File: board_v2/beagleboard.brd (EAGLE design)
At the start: 69.8 x 54.6 mm, 40 parts, among them U1 DWM1000, X1 5566-2, X2 04-JST-B4B-XH-A

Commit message: pullups
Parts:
- added R16, R17: 10k, rcl:R0805
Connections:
- net +5V: now also R16.2, R17.2
- net MLEN: now also R17.1
- net MREN: now also R16.1
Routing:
- net +5V: track 174.5 -> 185.0 mm
- net MLEN: track 40.1 -> 43.1 mm
- net MREN: track 44.2 -> 47.0 mm
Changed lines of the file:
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@@
 <element name="R14" library="rcl" package="R0805" value="" x="33.02" y="46.99" rot="R270"/>
 <element name="R15" library="rcl" package="R0805" value="" x="31.115" y="46.99" rot="R90"/>
+<element name="R16" library="rcl" package="R0805" value="10k" x="26.3525" y="20.0025" rot="R180"/>
+<element name="R17" library="rcl" package="R0805" value="10k" x="16.51" y="37.1475" rot="R270"/>
 </elements>
 <signals>
@@
 <wire x1="17.145" y1="10.4775" x2="12.7" y2="6.0325" width="0.8128" layer="16"/>
 <wire x1="12.7" y1="6.0325" x2="12.7" y2="5.08" width="0.8128" layer="16"/>
+<contactref element="R16" pad="2"/>
+<contactref element="R17" pad="2"/>
+<wire x1="16.51" y1="36.1975" x2="17.465" y2="36.1975" width="0.4064" layer="1"/>
+<wire x1="17.465" y1="36.1975" x2="17.78" y2="36.5125" width="0.4064" layer="1"/>
+<wire x1="17.78" y1="36.5125" x2="22.86" y2="36.5125" width="0.4064" layer="1"/>
+<wire x1="22.86" y1="36.5125" x2="23.8125" y2="37.465" width="0.4064" layer="1"/>
+<wire x1="25.4025" y1="20.0025" x2="25.4025" y2="22.3545" width="0.4064" layer="1"/>
+<wire x1="25.4025" y1="22.3545" x2="25.5905" y2="22.5425" width="0.4064" layer="1"/>
 </signal>
 <signal name="CSN">
@@
 <wire x1="40.3225" y1="39.0525" x2="20.6375" y2="39.0525" width="0.4064" layer="1"/>
 <wire x1="20.6375" y1="39.0525" x2="19.3675" y2="37.7825" width="0.4064" layer="1"/>
+<contactref element="R17" pad="1"/>
+<wire x1="16.51" y1="38.0975" x2="19.0525" y2="38.0975" width="0.4064" layer="1"/>
+<wire x1="19.0525" y1="38.0975" x2="19.3675" y2="37.7825" width="0.4064" layer="1"/>
 </signal>
 <signal name="MOSI">
@@
 <wire x1="32.385" y1="20.955" x2="31.4325" y2="20.0025" width="0.4064" layer="1"/>
 <wire x1="31.4325" y1="20.0025" x2="30.1625" y2="20.0025" width="0.4064" layer="1"/>
+<contactref element="R16" pad="1"/>
+<wire x1="27.3025" y1="20.0025" x2="30.1625" y2="20.0025" width="0.4064" layer="1"/>
 </signal>
 <signal name="DWMRES">

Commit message: values
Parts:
- R10, R12, R14: value (none) -> 1,1k
- R11, R13, R15: value (none) -> 2k
- R4, R5, R6: value (none) -> 1k
- R7, R8, R9: value (none) -> 1,5k
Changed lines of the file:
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@@
 <element name="SENS2" library="libsjst_eph" package="B4B-PH-K-S" value="4PIN" x="20.32" y="43.18" rot="R180"/>
 <element name="X2" library="bt_con-jst-xh" package="B4B-XH" value="04-JST-B4B-XH-A" x="69.85" y="34.925" rot="R90"/>
-<element name="R4" library="rcl" package="R0805" value="" x="60.0075" y="33.655"/>
-<element name="R5" library="rcl" package="R0805" value="" x="60.0075" y="31.75"/>
-<element name="R6" library="rcl" package="R0805" value="" x="58.1025" y="27.94"/>
-<element name="R7" library="rcl" package="R0805" value="" x="64.77" y="29.845"/>
-<element name="R8" library="rcl" package="R0805" value="" x="64.77" y="31.75"/>
-<element name="R9" library="rcl" package="R0805" value="" x="64.77" y="33.655"/>
+<element name="R4" library="rcl" package="R0805" value="1k" x="60.0075" y="33.655"/>
+<element name="R5" library="rcl" package="R0805" value="1k" x="60.0075" y="31.75"/>
+<element name="R6" library="rcl" package="R0805" value="1k" x="58.1025" y="27.94"/>
+<element name="R7" library="rcl" package="R0805" value="1,5k" x="64.77" y="29.845"/>
+<element name="R8" library="rcl" package="R0805" value="1,5k" x="64.77" y="31.75"/>
+<element name="R9" library="rcl" package="R0805" value="1,5k" x="64.77" y="33.655"/>
 <element name="SENS1" library="libsjst_eph" package="B4B-PH-K-S" value="4PIN" x="8.5725" y="43.18" rot="R180"/>
 <element name="SENS3" library="libsjst_eph" package="B4B-PH-K-S" value="4PIN" x="32.0675" y="43.18" rot="R180"/>
@@
 <element name="SJ5" library="jumper" package="SJ" value="" x="26.3525" y="25.0825" rot="R180"/>
 <element name="SJ6" library="jumper" package="SJ" value="" x="26.3525" y="27.6225" rot="R180"/>
-<element name="R10" library="rcl" package="R0805" value="" x="9.525" y="46.99" rot="R270"/>
-<element name="R11" library="rcl" package="R0805" value="" x="7.62" y="46.99" rot="R90"/>
-<element name="R12" library="rcl" package="R0805" value="" x="21.2725" y="46.99" rot="R270"/>
-<element name="R13" library="rcl" package="R0805" value="" x="19.3675" y="46.99" rot="R90"/>
-<element name="R14" library="rcl" package="R0805" value="" x="33.02" y="46.99" rot="R270"/>
-<element name="R15" library="rcl" package="R0805" value="" x="31.115" y="46.99" rot="R90"/>
+<element name="R10" library="rcl" package="R0805" value="1,1k" x="9.525" y="46.99" rot="R270"/>
+<element name="R11" library="rcl" package="R0805" value="2k" x="7.62" y="46.99" rot="R90"/>
+<element name="R12" library="rcl" package="R0805" value="1,1k" x="21.2725" y="46.99" rot="R270"/>
+<element name="R13" library="rcl" package="R0805" value="2k" x="19.3675" y="46.99" rot="R90"/>
+<element name="R14" library="rcl" package="R0805" value="1,1k" x="33.02" y="46.99" rot="R270"/>
+<element name="R15" library="rcl" package="R0805" value="2k" x="31.115" y="46.99" rot="R90"/>
 <element name="R16" library="rcl" package="R0805" value="10k" x="26.3525" y="20.0025" rot="R180"/>
 <element name="R17" library="rcl" package="R0805" value="10k" x="16.51" y="37.1475" rot="R270"/>

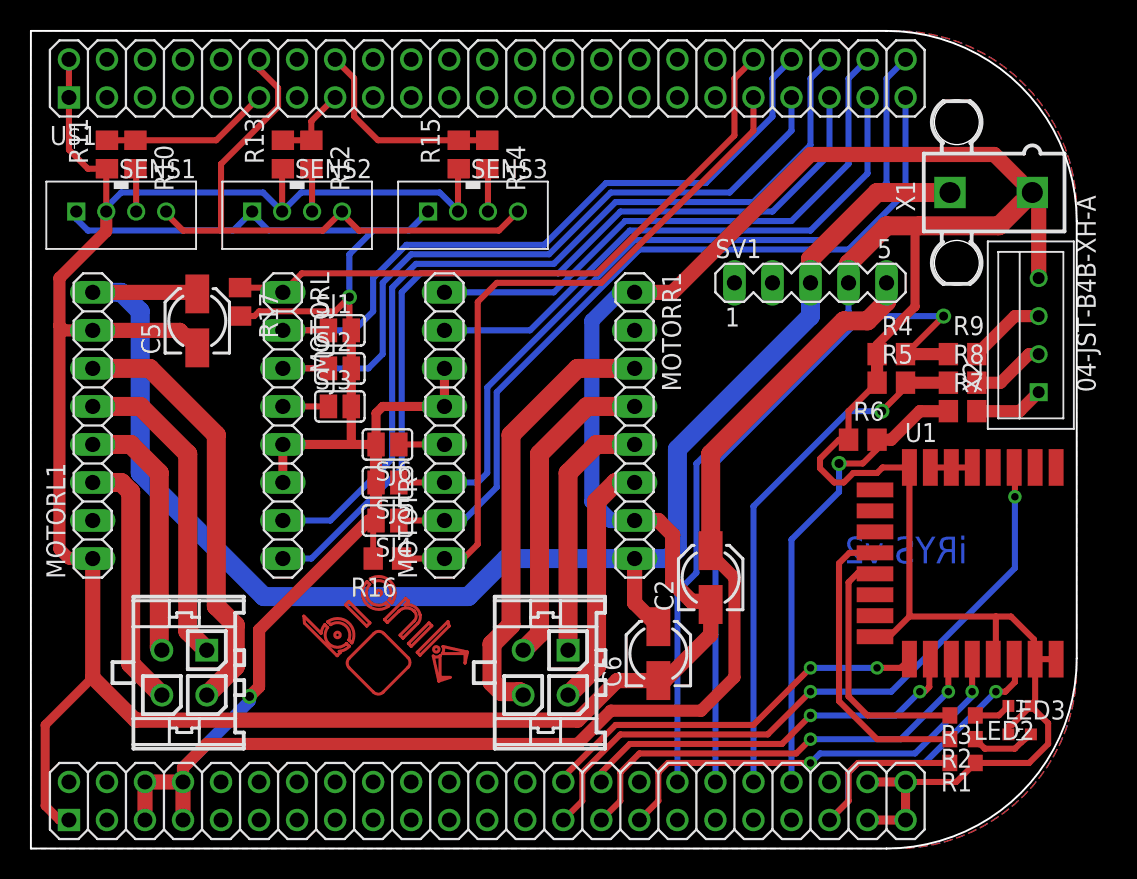
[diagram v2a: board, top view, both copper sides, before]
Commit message: right sonar wires
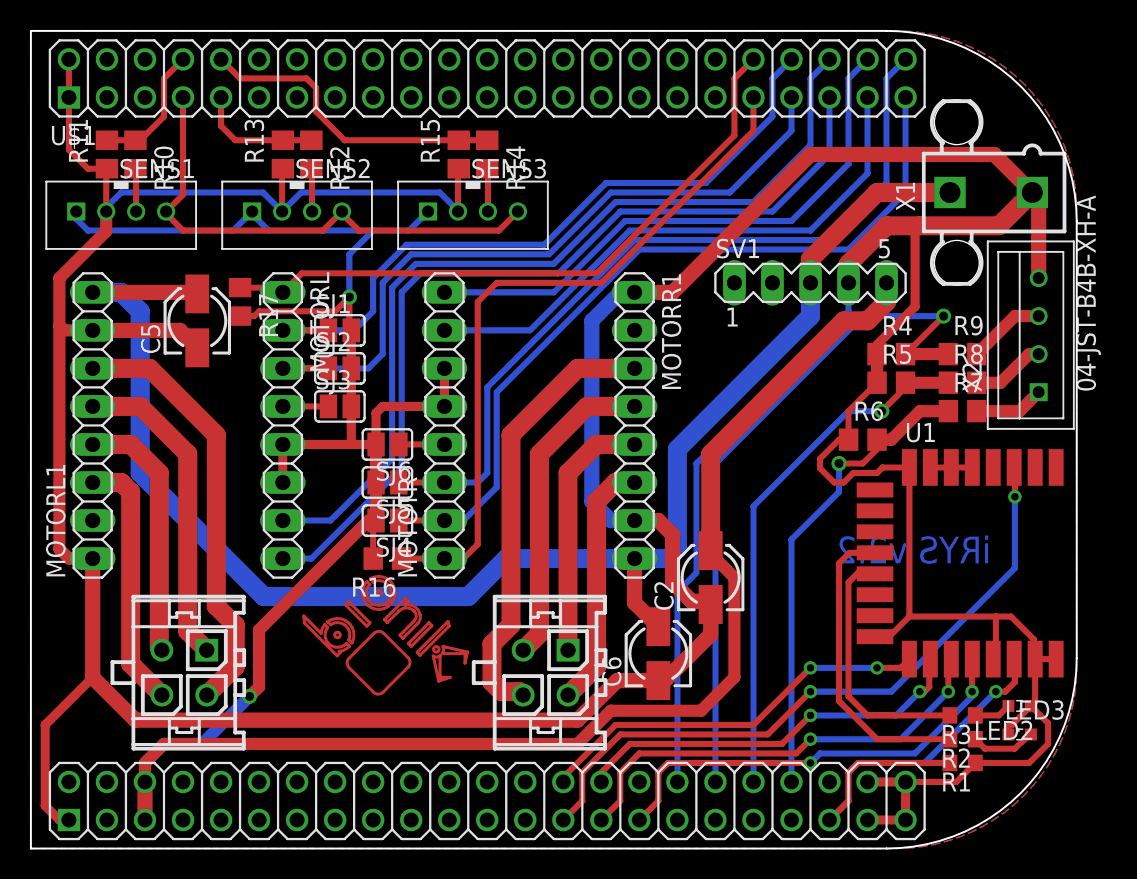
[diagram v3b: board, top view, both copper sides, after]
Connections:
- removed net N$42: U$1.9
- new net N$26: U$1.15
- new net SYS_5V: U$1.53
- net +5V: no longer U$1.53, U$1.54
- net D1ECHO: now also U$1.8; no longer U$1.11
- net D2ECHO: now also U$1.9; no longer U$1.15
- net D3ECHO: now also U$1.10; no longer U$1.16
- net N$20: now also U$1.12; no longer U$1.7
- net N$22: now also U$1.16; no longer U$1.8
- net N$23: now also U$1.11; no longer U$1.10
- net TRIG: now also U$1.7; no longer U$1.12
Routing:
- net D3ECHO: track 13.9 -> 20.9 mm
- net TRIG: track 39.3 -> 33.9 mm
- net D2ECHO: track 5.42 -> 8.33 mm
- net D1ECHO: track 11.3 -> 8.80 mm
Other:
- board text added: "iRYS v2.2"
- board text removed: "iRYS v2"
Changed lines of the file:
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@@
 <board>
 <plain>
-<text x="65.0875" y="19.685" size="1.778" layer="16" rot="MR0">iRYS v2</text>
+<text x="66.675" y="19.685" size="1.778" layer="16" rot="MR0">iRYS v2.2</text>
 <circle x="29.617984375" y="13.93655" radius="0.182878125" width="0.203" layer="1"/>
 <circle x="25.77360625" y="17.704809375" radius="0.18288125" width="0.203" layer="1"/>
@@
 <contactref element="MOTOTR" pad="5"/>
 <contactref element="U$1" pad="52"/>
-<contactref element="U$1" pad="54"/>
 <contactref element="U$1" pad="51"/>
-<contactref element="U$1" pad="53"/>
 <wire x1="30.1625" y1="30.1625" x2="30.1625" y2="32.7025" width="0.6096" layer="1"/>
 <contactref element="C2" pad="+"/>
@@
 <wire x1="47.9425" y1="26.9875" x2="47.9425" y2="20.5325" width="1.27" layer="1"/>
 <wire x1="10.16" y1="2.54" x2="10.16" y2="5.08" width="1.016" layer="1"/>
-<wire x1="10.16" y1="5.08" x2="12.7" y2="5.08" width="1.016" layer="1"/>
-<wire x1="12.7" y1="5.08" x2="12.7" y2="2.54" width="1.016" layer="1"/>
 <wire x1="25.5905" y1="22.5425" x2="25.5905" y2="25.0825" width="0.8128" layer="1"/>
 <wire x1="25.5905" y1="25.0825" x2="25.5905" y2="27.6225" width="0.8128" layer="1"/>
@@
 <wire x1="47.3075" y1="9.8425" x2="41.275" y2="9.8425" width="0.8128" layer="1"/>
 <wire x1="41.275" y1="9.8425" x2="39.0525" y2="7.62" width="0.8128" layer="1"/>
-<wire x1="39.0525" y1="7.62" x2="14.2875" y2="7.62" width="0.8128" layer="1"/>
-<wire x1="14.2875" y1="7.62" x2="12.7" y2="6.0325" width="0.8128" layer="1"/>
-<wire x1="12.7" y1="6.0325" x2="12.7" y2="5.08" width="0.8128" layer="1"/>
+<wire x1="39.0525" y1="7.62" x2="11.43" y2="7.62" width="0.8128" layer="1"/>
 <wire x1="25.5905" y1="22.5425" x2="25.0825" y2="22.5425" width="0.8128" layer="1"/>
 <wire x1="25.0825" y1="22.5425" x2="17.78" y2="15.24" width="0.8128" layer="1"/>
@@
 <wire x1="17.78" y1="11.43" x2="17.145" y2="10.795" width="0.8128" layer="1"/>
 <via x="17.145" y="10.795" extent="1-16" drill="0.6"/>
-<wire x1="17.145" y1="10.795" x2="17.145" y2="10.4775" width="0.8128" layer="16"/>
-<wire x1="17.145" y1="10.4775" x2="12.7" y2="6.0325" width="0.8128" layer="16"/>
-<wire x1="12.7" y1="6.0325" x2="12.7" y2="5.08" width="0.8128" layer="16"/>
 <contactref element="R16" pad="2"/>
 <contactref element="R17" pad="2"/>
@@
 <wire x1="25.4025" y1="20.0025" x2="25.4025" y2="22.3545" width="0.4064" layer="1"/>
 <wire x1="25.4025" y1="22.3545" x2="25.5905" y2="22.5425" width="0.4064" layer="1"/>
+<wire x1="11.43" y1="7.62" x2="10.16" y2="6.35" width="0.8128" layer="1"/>
+<wire x1="10.16" y1="6.35" x2="10.16" y2="5.08" width="0.8128" layer="1"/>
+<wire x1="17.145" y1="10.795" x2="13.97" y2="7.62" width="0.8128" layer="16"/>
+<wire x1="13.97" y1="7.62" x2="11.43" y2="7.62" width="0.8128" layer="16"/>
+<wire x1="11.43" y1="7.62" x2="10.16" y2="6.35" width="0.8128" layer="16"/>
+<wire x1="10.16" y1="6.35" x2="10.16" y2="5.08" width="0.8128" layer="16"/>
 </signal>
 <signal name="CSN">
@@
 <contactref element="U$1" pad="6"/>
 </signal>
-<signal name="N$22">
-<contactref element="U$1" pad="8"/>
-</signal>
-<signal name="N$23">
-<contactref element="U$1" pad="10"/>
-</signal>
 <signal name="N$25">
 <contactref element="U$1" pad="14"/>
@@
 <contactref element="SENS2" pad="4"/>
 <contactref element="SENS3" pad="4"/>
-<contactref element="U$1" pad="12"/>
 <wire x1="11.5725" y1="43.18" x2="11.5725" y2="43.0375" width="0.4064" layer="1"/>
 <wire x1="11.5725" y1="43.0375" x2="12.7" y2="41.91" width="0.4064" layer="1"/>
-<wire x1="12.7" y1="41.91" x2="15.24" y2="41.91" width="0.4064" layer="1"/>
-<wire x1="15.24" y1="41.91" x2="22.05" y2="41.91" width="0.4064" layer="1"/>
+<wire x1="12.7" y1="41.91" x2="22.05" y2="41.91" width="0.4064" layer="1"/>
 <wire x1="22.05" y1="41.91" x2="23.32" y2="43.18" width="0.4064" layer="1"/>
 <wire x1="23.32" y1="43.18" x2="23.32" y2="43.0375" width="0.4064" layer="1"/>
@@
 <wire x1="24.4475" y1="41.91" x2="33.7975" y2="41.91" width="0.4064" layer="1"/>
 <wire x1="33.7975" y1="41.91" x2="35.0675" y2="43.18" width="0.4064" layer="1"/>
-<wire x1="17.78" y1="53.34" x2="17.78" y2="52.705" width="0.4064" layer="1"/>
-<wire x1="17.78" y1="52.705" x2="19.05" y2="51.435" width="0.4064" layer="1"/>
-<wire x1="19.05" y1="51.435" x2="19.05" y2="50.165" width="0.4064" layer="1"/>
-<wire x1="19.05" y1="50.165" x2="15.24" y2="46.355" width="0.4064" layer="1"/>
-<wire x1="15.24" y1="46.355" x2="15.24" y2="41.91" width="0.4064" layer="1"/>
+<contactref element="U$1" pad="7"/>
+<wire x1="12.7" y1="50.8" x2="12.7" y2="44.3075" width="0.4064" layer="1"/>
+<wire x1="12.7" y1="44.3075" x2="11.5725" y2="43.18" width="0.4064" layer="1"/>
 </signal>
 <signal name="D4ECHO">
@@
 <signal name="N$19">
 <contactref element="U$1" pad="5"/>
-</signal>
-<signal name="N$20">
-<contactref element="U$1" pad="7"/>
-</signal>
-<signal name="N$42">
-<contactref element="U$1" pad="9"/>
 </signal>
 <signal name="N$44">
@@
 <contactref element="R10" pad="1"/>
 <contactref element="R11" pad="2"/>
-<contactref element="U$1" pad="11"/>
-<wire x1="9.525" y1="47.94" x2="14.92" y2="47.94" width="0.4064" layer="1"/>
-<wire x1="14.92" y1="47.94" x2="17.78" y2="50.8" width="0.4064" layer="1"/>
 <wire x1="7.62" y1="47.94" x2="9.525" y2="47.94" width="0.4064" layer="1"/>
+<contactref element="U$1" pad="8"/>
+<wire x1="9.525" y1="47.94" x2="9.84" y2="47.94" width="0.4064" layer="1"/>
+<wire x1="9.84" y1="47.94" x2="11.43" y2="49.53" width="0.4064" layer="1"/>
+<wire x1="11.43" y1="49.53" x2="11.43" y2="52.07" width="0.4064" layer="1"/>
+<wire x1="11.43" y1="52.07" x2="12.7" y2="53.34" width="0.4064" layer="1"/>
 </signal>
 <signal name="N$78">
@@
 <contactref element="R12" pad="1"/>
 <contactref element="R13" pad="2"/>
-<contactref element="U$1" pad="15"/>
-<wire x1="21.2725" y1="47.94" x2="21.2725" y2="49.2125" width="0.4064" layer="1"/>
-<wire x1="21.2725" y1="49.2125" x2="22.86" y2="50.8" width="0.4064" layer="1"/>
 <wire x1="21.2725" y1="47.94" x2="19.3675" y2="47.94" width="0.4064" layer="1"/>
+<contactref element="U$1" pad="9"/>
+<wire x1="19.3675" y1="47.94" x2="16.195" y2="47.94" width="0.4064" layer="1"/>
+<wire x1="16.195" y1="47.94" x2="15.24" y2="48.895" width="0.4064" layer="1"/>
+<wire x1="15.24" y1="48.895" x2="15.24" y2="50.8" width="0.4064" layer="1"/>
 </signal>
 <signal name="N$80">
@@
 <contactref element="R14" pad="1"/>
 <contactref element="R15" pad="2"/>
-<contactref element="U$1" pad="16"/>
-<wire x1="31.115" y1="47.94" x2="25.72" y2="47.94" width="0.4064" layer="1"/>
-<wire x1="25.72" y1="47.94" x2="24.13" y2="49.53" width="0.4064" layer="1"/>
-<wire x1="24.13" y1="49.53" x2="24.13" y2="52.07" width="0.4064" layer="1"/>
-<wire x1="24.13" y1="52.07" x2="22.86" y2="53.34" width="0.4064" layer="1"/>
+<wire x1="31.115" y1="47.94" x2="23.4975" y2="47.94" width="0.4064" layer="1"/>
 <wire x1="33.02" y1="47.94" x2="31.115" y2="47.94" width="0.4064" layer="1"/>
+<contactref element="U$1" pad="10"/>
+<wire x1="23.4975" y1="47.94" x2="21.59" y2="49.8475" width="0.4064" layer="1"/>
+<wire x1="21.59" y1="49.8475" x2="21.59" y2="51.435" width="0.4064" layer="1"/>
+<wire x1="21.59" y1="51.435" x2="20.955" y2="52.07" width="0.4064" layer="1"/>
+<wire x1="20.955" y1="52.07" x2="16.51" y2="52.07" width="0.4064" layer="1"/>
+<wire x1="16.51" y1="52.07" x2="15.24" y2="53.34" width="0.4064" layer="1"/>
 </signal>
 <signal name="N$77">
@@
 <wire x1="26.451396875" y1="16.841890625" x2="26.260896875" y2="17.041621875" width="0.203" layer="1"/>
 </signal>
+<signal name="N$20">
+<contactref element="U$1" pad="12"/>
+</signal>
+<signal name="N$22">
+<contactref element="U$1" pad="16"/>
+</signal>
+<signal name="N$23">
+<contactref element="U$1" pad="11"/>
+</signal>
+<signal name="N$26">
+<contactref element="U$1" pad="15"/>
+</signal>
+<signal name="SYS_5V">
+<contactref element="U$1" pad="53"/>
+</signal>
 </signals>
